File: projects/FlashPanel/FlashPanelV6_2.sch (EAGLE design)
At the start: 28 parts

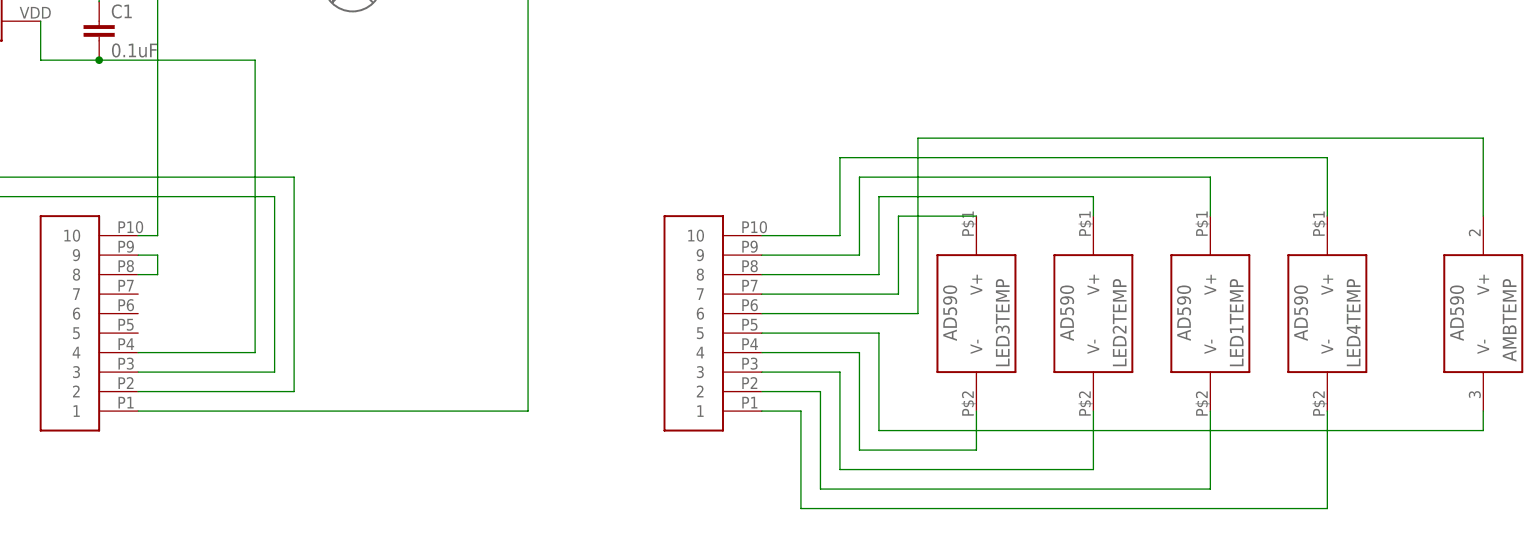
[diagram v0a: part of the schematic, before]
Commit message: Small updates to Flash Panel V6.2
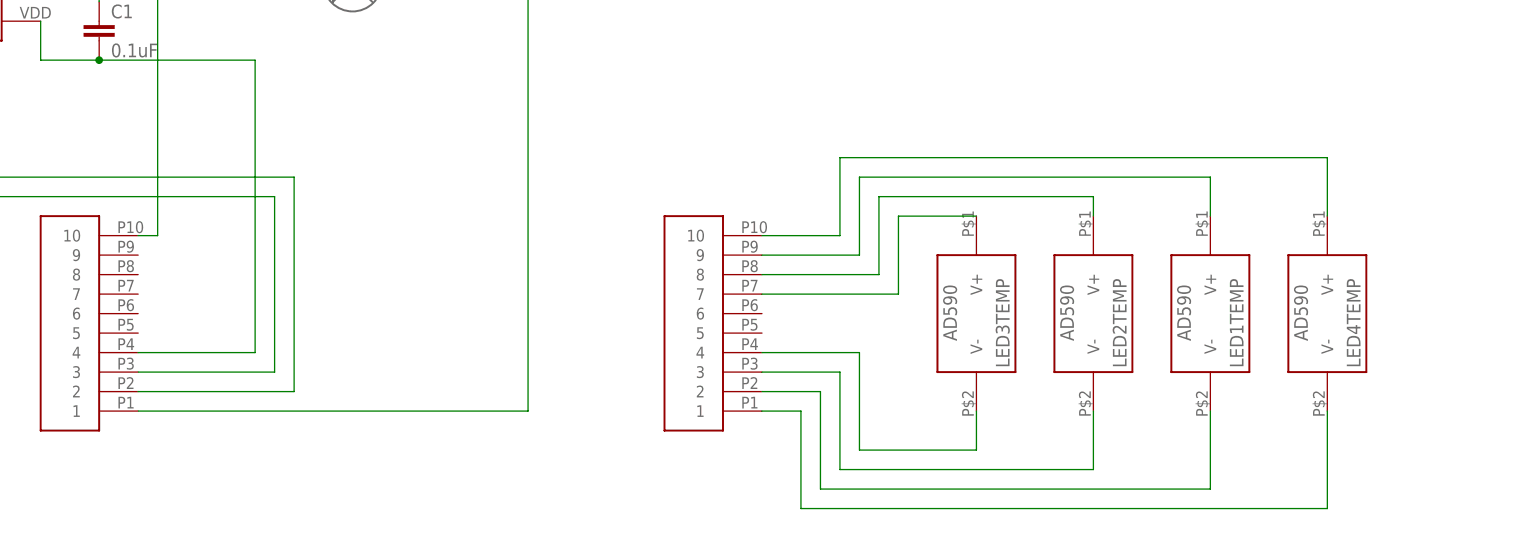
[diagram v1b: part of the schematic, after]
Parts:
- removed AMBTEMP: AD590, CNTRL_BOARD:AD590-SOIC-8
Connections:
- removed net N$26: AMBTEMP.V-, TEMPCONNM.5
- removed net N$27: AMBTEMP.V+, TEMPCONNM.6
- removed net TEST: CONN13M.8, CONN13M.9
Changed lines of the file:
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@@
 <?xml version="1.0" encoding="utf-8"?>
 <!DOCTYPE eagle SYSTEM "eagle.dtd">
-<eagle version="7.6.0">
+<eagle version="7.7.0">
 <drawing>
 <settings>
@@
 <part name="LED1TEMP" library="CNTRL_BOARD" deviceset="AD590-TH" device=""/>
 <part name="LED4TEMP" library="CNTRL_BOARD" deviceset="AD590-TH" device=""/>
-<part name="AMBTEMP" library="CNTRL_BOARD" deviceset="AD590-SOIC-8" device="" value="AD590"/>
 </parts>
 <sheets>
@@
 <instance part="LED1TEMP" gate="G$1" x="320.04" y="43.18" rot="R270"/>
 <instance part="LED4TEMP" gate="G$1" x="335.28" y="43.18" rot="R270"/>
-<instance part="AMBTEMP" gate="G$1" x="355.6" y="43.18" rot="R270"/>
 </instances>
 <busses>
@@
 </segment>
 </net>
-<net name="N$26" class="0">
-<segment>
-<pinref part="TEMPCONNM" gate="G$1" pin="5"/>
-<wire x1="261.62" y1="40.64" x2="276.86" y2="40.64" width="0.1524" layer="91"/>
-<wire x1="276.86" y1="40.64" x2="276.86" y2="27.94" width="0.1524" layer="91"/>
-<wire x1="276.86" y1="27.94" x2="355.6" y2="27.94" width="0.1524" layer="91"/>
-<pinref part="AMBTEMP" gate="G$1" pin="V-"/>
-<wire x1="355.6" y1="27.94" x2="355.6" y2="30.48" width="0.1524" layer="91"/>
-</segment>
-</net>
-<net name="N$27" class="0">
-<segment>
-<pinref part="AMBTEMP" gate="G$1" pin="V+"/>
-<wire x1="355.6" y1="55.88" x2="355.6" y2="66.04" width="0.1524" layer="91"/>
-<wire x1="355.6" y1="66.04" x2="281.94" y2="66.04" width="0.1524" layer="91"/>
-<wire x1="281.94" y1="66.04" x2="281.94" y2="43.18" width="0.1524" layer="91"/>
-<pinref part="TEMPCONNM" gate="G$1" pin="6"/>
-<wire x1="281.94" y1="43.18" x2="261.62" y2="43.18" width="0.1524" layer="91"/>
-</segment>
-</net>
-<net name="TEST" class="0">
-<segment>
-<pinref part="CONN13M" gate="G$1" pin="9"/>
-<wire x1="180.34" y1="50.8" x2="182.88" y2="50.8" width="0.1524" layer="91"/>
-<wire x1="182.88" y1="50.8" x2="182.88" y2="48.26" width="0.1524" layer="91"/>
-<pinref part="CONN13M" gate="G$1" pin="8"/>
-<wire x1="182.88" y1="48.26" x2="180.34" y2="48.26" width="0.1524" layer="91"/>
-</segment>
-</net>

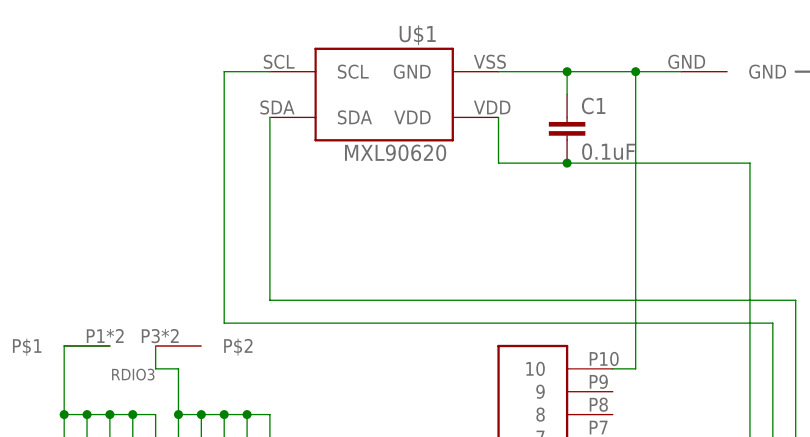
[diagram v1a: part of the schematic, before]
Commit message: Cleaned up Git tracked files. Changes/additions to libraries. Addition of missing LED library part. Began Battery Board layout.
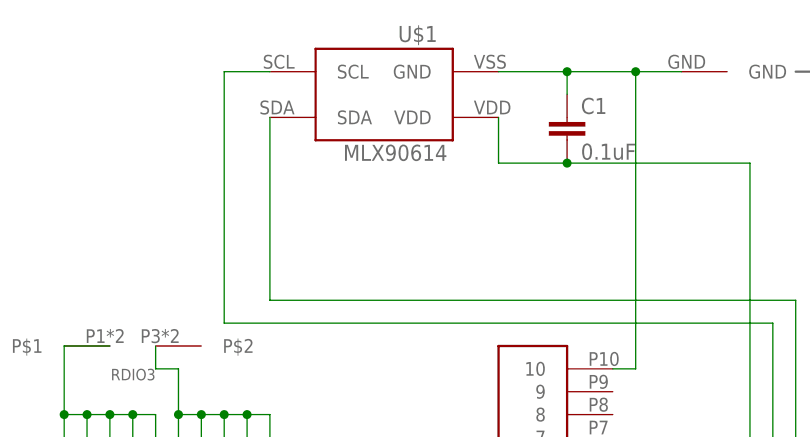
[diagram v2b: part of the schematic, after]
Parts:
- U$1: value MXL90620 -> MXL90614; device CNTRL_BOARD:MXL90620 -> CNTRL_BOARD:MXL90614
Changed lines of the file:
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@@
 <part name="LED4+M" library="cxm27" deviceset="10PINMALE" device=""/>
 <part name="LED4-M" library="cxm27" deviceset="10PINMALE" device=""/>
-<part name="U$1" library="CNTRL_BOARD" deviceset="MXL90620" device=""/>
+<part name="U$1" library="CNTRL_BOARD" deviceset="MXL90614" device=""/>
 <part name="ANTDEP1M" library="cxm27" deviceset="10PINMALE" device=""/>
 <part name="ANTDEP2M" library="cxm27" deviceset="10PINMALE" device=""/>

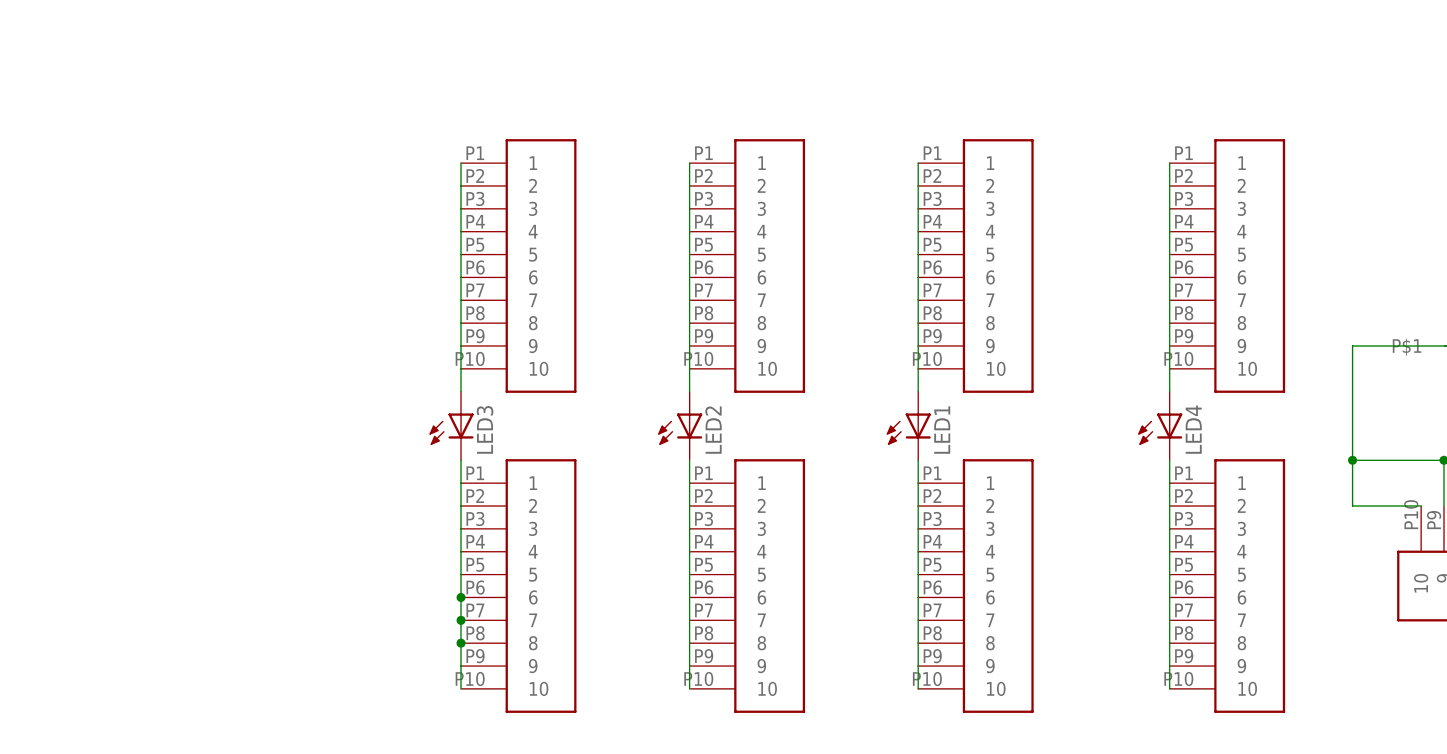
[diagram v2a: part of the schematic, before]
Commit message: Updates to Radio Adapter Board, Driver Board, Flash Panel. Somebody forgot to commit for a whole week or so....
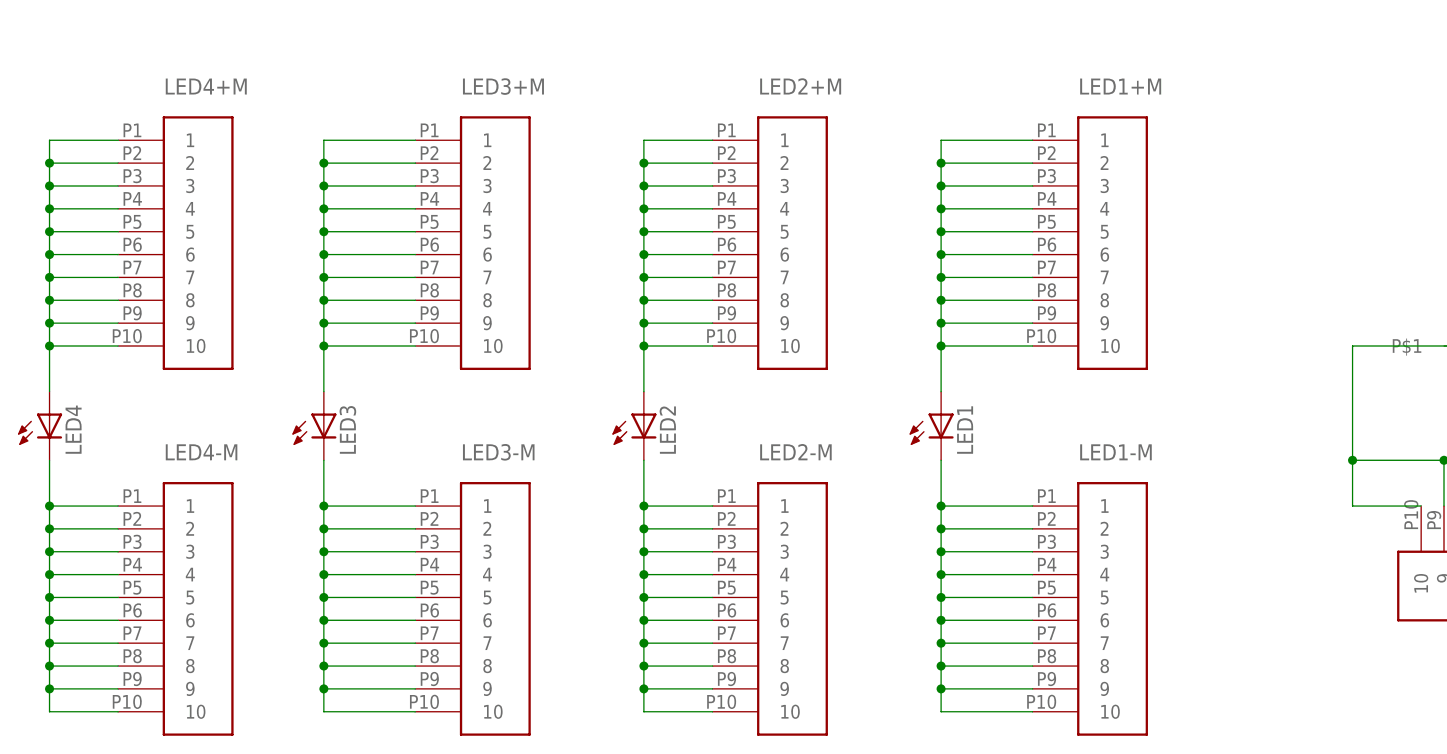
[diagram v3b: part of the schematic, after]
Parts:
- LED1, LED2, LED3, LED4: device cxm27:CXM27 -> chm27:CXM27
- LED1+M, LED1-M, LED2+M, LED2-M, LED3+M, LED3-M, LED4+M, LED4-M: device cxm27:10PINMALE -> chm27:10PINMALE
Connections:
- net N$1 renamed LED3P
- net N$2 renamed LED3M
- net N$7 renamed LED4M
- net N$8 renamed LED4P
- removed net N$3: LED2+M.1, LED2+M.10, LED2+M.2, LED2+M.3, LED2+M.4, LED2+M.5, LED2+M.6, LED2+M.7, LED2+M.8, LED2+M.9, LED2.C
- removed net N$4: LED2-M.1, LED2-M.10, LED2-M.2, LED2-M.3, LED2-M.4, LED2-M.5, LED2-M.6, LED2-M.7, LED2-M.8, LED2-M.9, LED2.A
- removed net N$5: LED1+M.1, LED1+M.10, LED1+M.2, LED1+M.3, LED1+M.4, LED1+M.5, LED1+M.6, LED1+M.7, LED1+M.8, LED1+M.9, LED1.C
- removed net N$6: LED1-M.1, LED1-M.10, LED1-M.2, LED1-M.3, LED1-M.4, LED1-M.5, LED1-M.6, LED1-M.7, LED1-M.8, LED1-M.9, LED1.A
- new net LED1M: LED1-M.1, LED1-M.10, LED1-M.2, LED1-M.3, LED1-M.4, LED1-M.5, LED1-M.6, LED1-M.7, LED1-M.8, LED1-M.9, LED1.C
- new net LED1P: LED1+M.1, LED1+M.10, LED1+M.2, LED1+M.3, LED1+M.4, LED1+M.5, LED1+M.6, LED1+M.7, LED1+M.8, LED1+M.9, LED1.A
- new net LED2M: LED2-M.1, LED2-M.10, LED2-M.2, LED2-M.3, LED2-M.4, LED2-M.5, LED2-M.6, LED2-M.7, LED2-M.8, LED2-M.9, LED2.C
- new net LED2P: LED2+M.1, LED2+M.10, LED2+M.2, LED2+M.3, LED2+M.4, LED2+M.5, LED2+M.6, LED2+M.7, LED2+M.8, LED2+M.9, LED2.A
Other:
- moved on the sheet: LED1, LED2, LED3, LED4

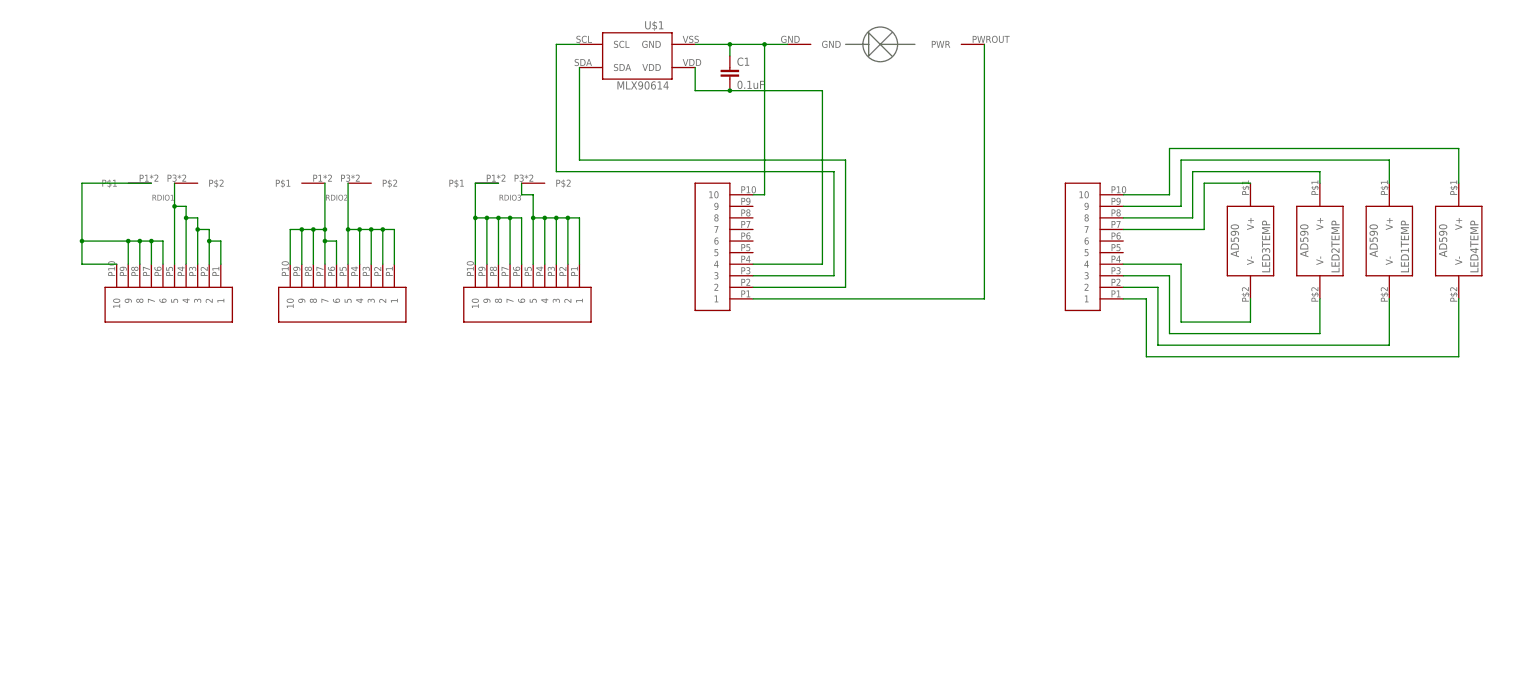
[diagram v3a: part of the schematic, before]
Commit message: Completed all changes to Flash Panel and Driver Board. Additional library changes and additions for antenna deployment detection circuitry.
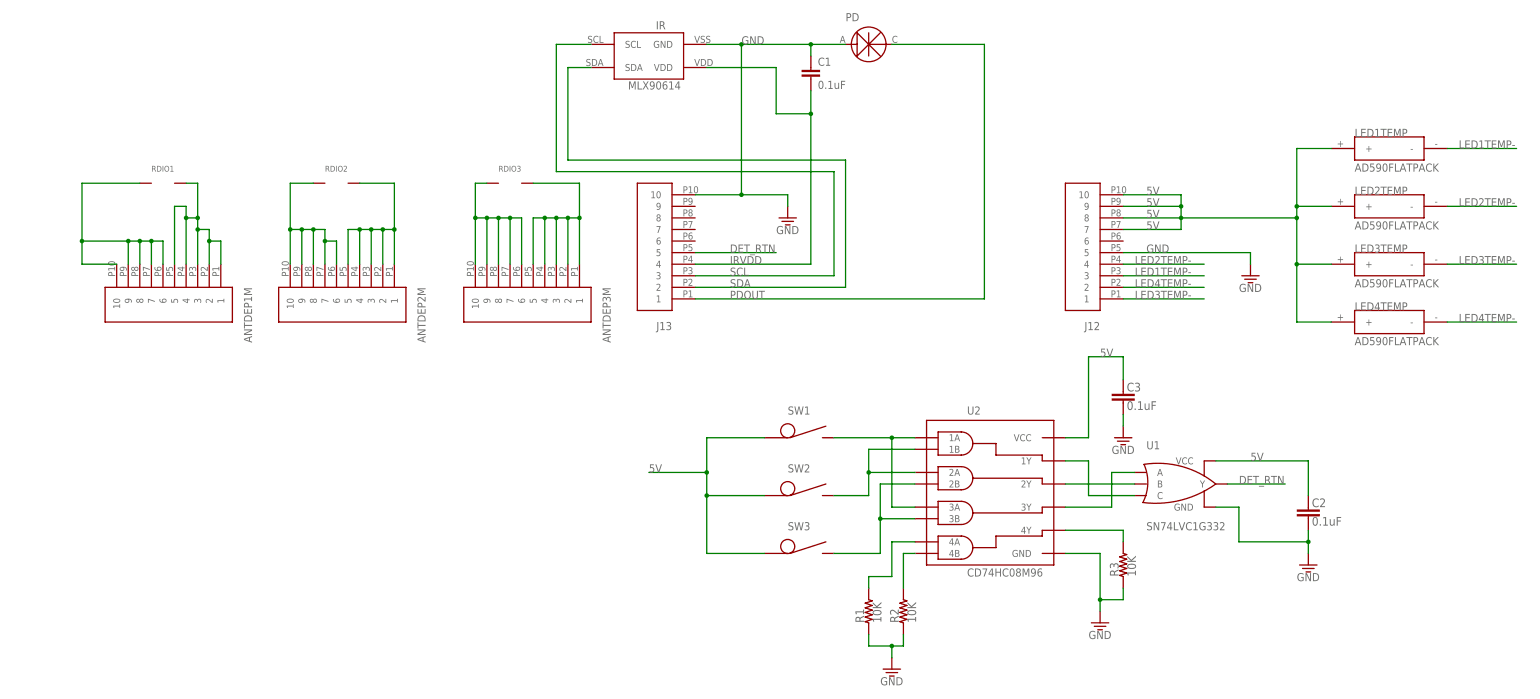
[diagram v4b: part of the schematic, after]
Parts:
- removed CONN13M, TEMPCONNM: (no value), cxm27:10PINMALE
- removed U$1: MXL90614, CNTRL_BOARD:MXL90614
- removed U$2: PHOTODETECTBOTTOM, solarcellnew:PHOTODETECTBOTTOM
- added C2, C3: 0.1uF, BrownSpaceEngineering:CAP0805
- added IR: MXL90614, CNTRL_BOARD:MXL90614
- added J12, J13: (no value), chm27:10PINMALE
- added PD: TEMD6200, BrownSpaceEngineering:TEMD6200
- added R1, R2, R3: 10K, BrownSpaceEngineering:RES0805
- added SW1, SW2, SW3: SW-DETECT, BrownSpaceEngineering:SW-DETECT
- added U1: SN74LVC1G332, BrownSpaceEngineering:SN74LVC1G332
- added U2: CD74HC08M96, BrownSpaceEngineering:CD74HC08M96
- ANTDEP1M, ANTDEP2M, ANTDEP3M: device cxm27:10PINMALE -> chm27:10PINMALE
- LED1TEMP, LED2TEMP, LED3TEMP, LED4TEMP: value AD590-TH -> AD590FLATPACK; device CNTRL_BOARD:AD590-TH -> BrownSpaceEngineering:AD590FLATPACK
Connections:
- removed net 3V3: C1.2, CONN13M.4, U$1.VDD
- removed net N$10: ANTDEP1M.1, ANTDEP1M.2, ANTDEP1M.3, ANTDEP1M.4, ANTDEP1M.5, RDIO1.P$2
- removed net N$11: ANTDEP2M.10, ANTDEP2M.6, ANTDEP2M.7, ANTDEP2M.8, ANTDEP2M.9, RDIO2.P$1
- removed net N$12: ANTDEP2M.1, ANTDEP2M.2, ANTDEP2M.3, ANTDEP2M.4, ANTDEP2M.5, RDIO2.P$2
- removed net N$13: ANTDEP3M.10, ANTDEP3M.6, ANTDEP3M.7, ANTDEP3M.8, ANTDEP3M.9, RDIO3.P$1
- removed net N$14: ANTDEP3M.1, ANTDEP3M.2, ANTDEP3M.3, ANTDEP3M.4, ANTDEP3M.5, RDIO3.P$2
- removed net N$15: LED4TEMP.V-, TEMPCONNM.1
- removed net N$20: LED2TEMP.V-, TEMPCONNM.3
- removed net N$21: LED3TEMP.V-, TEMPCONNM.4
- removed net N$22: LED4TEMP.V+, TEMPCONNM.10
- removed net N$23: LED1TEMP.V+, TEMPCONNM.9
- removed net N$24: LED2TEMP.V+, TEMPCONNM.8
- removed net N$25: LED3TEMP.V+, TEMPCONNM.7
- removed net RDIO1: ANTDEP1M.10, ANTDEP1M.6, ANTDEP1M.7, ANTDEP1M.8, ANTDEP1M.9, RDIO1.P$1
- new net 5V: C2.P$1, C3.P$1, J12.10, J12.7, J12.8, J12.9, LED1TEMP.+, LED2TEMP.+, LED3TEMP.+, LED4TEMP.+, SW1.P$1, SW2.P$1, SW3.P$1, U1.VCC, U2.VCC
- new net DET_RTN: J13.5, U1.Y
- new net IRVDD: C1.2, IR.VDD, J13.4
- new net LED1TEMP-: J12.3, LED1TEMP.-
- new net LED2TEMP-: J12.4, LED2TEMP.-
- new net LED3TEMP-: J12.1, LED3TEMP.-
- new net LED4TEMP-: J12.2, LED4TEMP.-
- new net N$1: U1.C, U2.1Y
- new net N$2: U1.B, U2.2Y
- new net N$3: U1.A, U2.3Y
- new net N$4: SW1.P$2, U2.1A, U2.3A
- new net N$5: SW2.P$2, U2.1B, U2.2A
- new net N$6: SW3.P$2, U2.2B, U2.3B
- new net N$7: R2.2, U2.4B
- new net N$8: R1.2, U2.4A
- new net RDIO1+: ANTDEP1M.10, ANTDEP1M.6, ANTDEP1M.7, ANTDEP1M.8, ANTDEP1M.9, RDIO1.P$2
- new net RDIO1-: ANTDEP1M.1, ANTDEP1M.2, ANTDEP1M.3, ANTDEP1M.4, ANTDEP1M.5, RDIO1.P$1
- new net RDIO2+: ANTDEP2M.10, ANTDEP2M.6, ANTDEP2M.7, ANTDEP2M.8, ANTDEP2M.9, RDIO2.P$2
- new net RDIO2-: ANTDEP2M.1, ANTDEP2M.2, ANTDEP2M.3, ANTDEP2M.4, ANTDEP2M.5, RDIO2.P$1
- new net RDIO3+: ANTDEP3M.10, ANTDEP3M.6, ANTDEP3M.7, ANTDEP3M.8, ANTDEP3M.9, RDIO3.P$2
- new net RDIO3-: ANTDEP3M.1, ANTDEP3M.2, ANTDEP3M.3, ANTDEP3M.4, ANTDEP3M.5, RDIO3.P$1
- net GND: now also C2.P$2, C3.P$2, IR.GND, J12.5, J13.10, PD.A, R1.1, R2.1, R3.1, U1.GND, U2.GND; no longer CONN13M.10, U$1.GND, U$2.GND
- net N$16: now also R3.2, U2.4Y; no longer LED1TEMP.V-, TEMPCONNM.2
- net PDOUT: now also J13.1, PD.C; no longer CONN13M.1, U$2.PWR
- net SCL: now also IR.SCL, J13.3; no longer CONN13M.3, U$1.SCL
- net SDA: now also IR.SDA, J13.2; no longer CONN13M.2, U$1.SDA
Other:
- moved on the sheet: C1
